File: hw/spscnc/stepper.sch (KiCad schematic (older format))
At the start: 9 parts, among them J10 Conn_01x08_Female, J7 Limit_IF, J8 Conn_01x08_Female, J9 8P8C_4xShielded, SW1 SW_DIP_x04

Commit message: halfway changes to support additional axis and to extend over i2so
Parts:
- removed J10, J8: Conn_01x08_Female, Connector_PinHeader_2.54mm:PinHeader_1x08_P2.54mm_Vertical, symbol Connector:Conn_01x08_Female
- removed J7: Limit_IF, Connector_PinHeader_2.54mm:PinHeader_1x03_P2.54mm_Vertical, symbol Connector:Conn_01x03_Male
- removed J9: 8P8C_4xShielded, industrial000:rj45_R-RJ45S08P-B000_C386763, symbol industrial:8P8C_4xShielded
- removed R36, R37: 100, Resistor_SMD:R_0805_2012Metric_Pad1.20x1.40mm_HandSolder, symbol Device:R
- removed R38, R39: 10K, Resistor_SMD:R_0805_2012Metric_Pad1.20x1.40mm_HandSolder, symbol Device:R
- removed SW1: SW_DIP_x04, Package_DIP:DIP-8_W8.89mm_SMDSocket_LongPads, symbol Switch:SW_DIP_x04
- added J23: Conn_01x04, Connector_PinHeader_2.54mm:PinHeader_1x04_P2.54mm_Vertical, symbol Connector_Generic:Conn_01x04
- added J24: Conn_01x06, Connector_PinHeader_2.54mm:PinHeader_1x06_P2.54mm_Vertical, symbol Connector_Generic:Conn_01x06
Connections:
- net labels added: STEPPER_MISO, STEPPER_MOSI, STEPPER_SCK, ~ENABLE, ~STEPPER_CS
- net labels removed: +24V, 1A, 1B, 2A, 2B, ENABLE, First_Limiter, Second_Limiter
- wire segments 26 -> 6
- no-connect marks 1 -> 0
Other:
- note added: "Optional module.\n\nWhen getting prototypes from JLC, the second module can be reused from another prototype."
- note removed: "Legacy Steppers such as the DRV8825 polulu"

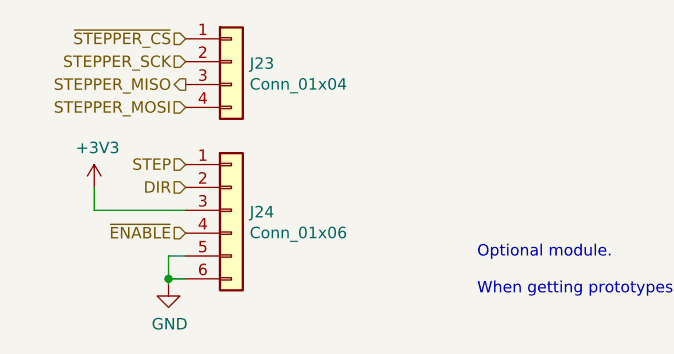
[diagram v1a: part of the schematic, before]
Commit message: added most corrections on the schematic for i2s operation.
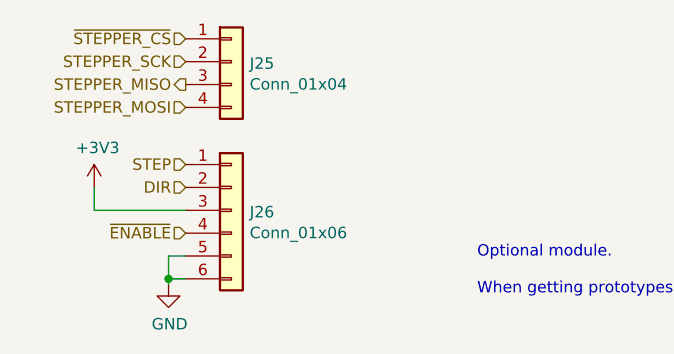
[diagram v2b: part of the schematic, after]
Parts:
- J23: jlcpcb DNP -> DNP008
- J24: jlcpcb DNP -> DNP562
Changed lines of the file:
@@
 $Descr A4 11693 8268
 encoding utf-8
-Sheet 16 16
+Sheet 17 17
 Title ""
 Date ""
@@
 U 1 1 6229F264
 P 4850 1750
-F 0 "J23" H 4930 1742 50  0000 L CNN
+AR Path="/6221509B/6229F264" Ref="J23"  Part="1"
+AR Path="/622F8C7E/6229F264" Ref="J25"  Part="1"
+F 0 "J25" H 4930 1742 50  0000 L CNN
 F 1 "Conn_01x04" H 4930 1651 50  0000 L CNN
 F 2 "Connector_PinHeader_2.54mm:PinHeader_1x04_P2.54mm_Vertical" H 4850 1750 50  0001 C CNN
 F 3 "~" H 4850 1750 50  0001 C CNN
-F 4 "DNP" H 4850 1750 50  0001 C CNN "jlcpcb"
+F 4 "DNP008" H 4850 1750 50  0001 C CNN "jlcpcb"
 	1    4850 1750
 	1    0    0    -1
@@
 U 1 1 6229FE51
 P 4850 2400
-F 0 "J24" H 4930 2392 50  0000 L CNN
+AR Path="/6221509B/6229FE51" Ref="J24"  Part="1"
+AR Path="/622F8C7E/6229FE51" Ref="J26"  Part="1"
+F 0 "J26" H 4930 2392 50  0000 L CNN
 F 1 "Conn_01x06" H 4930 2301 50  0000 L CNN
 F 2 "Connector_PinHeader_2.54mm:PinHeader_1x06_P2.54mm_Vertical" H 4850 2400 50  0001 C CNN
 F 3 "~" H 4850 2400 50  0001 C CNN
-F 4 "DNP" H 4850 2400 50  0001 C CNN "jlcpcb"
+F 4 "DNP562" H 4850 2400 50  0001 C CNN "jlcpcb"
 	1    4850 2400
 	1    0    0    -1
@@
 U 1 1 622A180C
 P 4250 2300
-F 0 "#PWR0246" H 4250 2150 50  0001 C CNN
+AR Path="/6221509B/622A180C" Ref="#PWR0246"  Part="1"
+AR Path="/622F8C7E/622A180C" Ref="#PWR0264"  Part="1"
+F 0 "#PWR0264" H 4250 2150 50  0001 C CNN
 F 1 "+3V3" H 4265 2473 50  0000 C CNN
 F 2 "" H 4250 2300 50  0001 C CNN
@@
 U 1 1 622A1D01
 P 4575 2725
-F 0 "#PWR0263" H 4575 2475 50  0001 C CNN
+AR Path="/6221509B/622A1D01" Ref="#PWR0263"  Part="1"
+AR Path="/622F8C7E/622A1D01" Ref="#PWR0265"  Part="1"
+F 0 "#PWR0265" H 4575 2475 50  0001 C CNN
 F 1 "GND" H 4580 2552 50  0000 C CNN
 F 2 "" H 4575 2725 50  0001 C CNN

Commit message: began routing of the i2so part
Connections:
- net STEPPER_MISO: now also J23.4 (Pin_4); no longer J23.3 (Pin_3)
- net STEPPER_MOSI: now also J23.3 (Pin_3); no longer J23.4 (Pin_4)
- net STEPPER_SCK: now also J23.1 (Pin_1); no longer J23.2 (Pin_2)
- net ~STEPPER_CS: now also J23.2 (Pin_2); no longer J23.1 (Pin_1)
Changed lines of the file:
@@
 $Descr A4 11693 8268
 encoding utf-8
-Sheet 17 17
+Sheet 16 17
 Title ""
 Date ""
@@
 Comment4 ""
 $EndDescr
+Text HLabel 4650 1750 0    50   Input ~ 0
+~STEPPER_CS
+Text HLabel 4650 1950 0    50   Output ~ 0
+STEPPER_MISO
+Text HLabel 4650 1850 0    50   Input ~ 0
+STEPPER_MOSI
 Text HLabel 4650 1650 0    50   Input ~ 0
-~STEPPER_CS
-Text HLabel 4650 1850 0    50   Output ~ 0
-STEPPER_MISO
-Text HLabel 4650 1950 0    50   Input ~ 0
-STEPPER_MOSI
-Text HLabel 4650 1750 0    50   Input ~ 0
 STEPPER_SCK
 Text HLabel 4650 2500 0    50   Input ~ 0
